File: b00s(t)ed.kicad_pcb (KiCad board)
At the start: 2 copper layers, 21 x 19 mm, 10 parts, among them Q1 IRF7739L1, Q2 2N7002W, U1 LM5050-1, U2 NSI50010YT1G

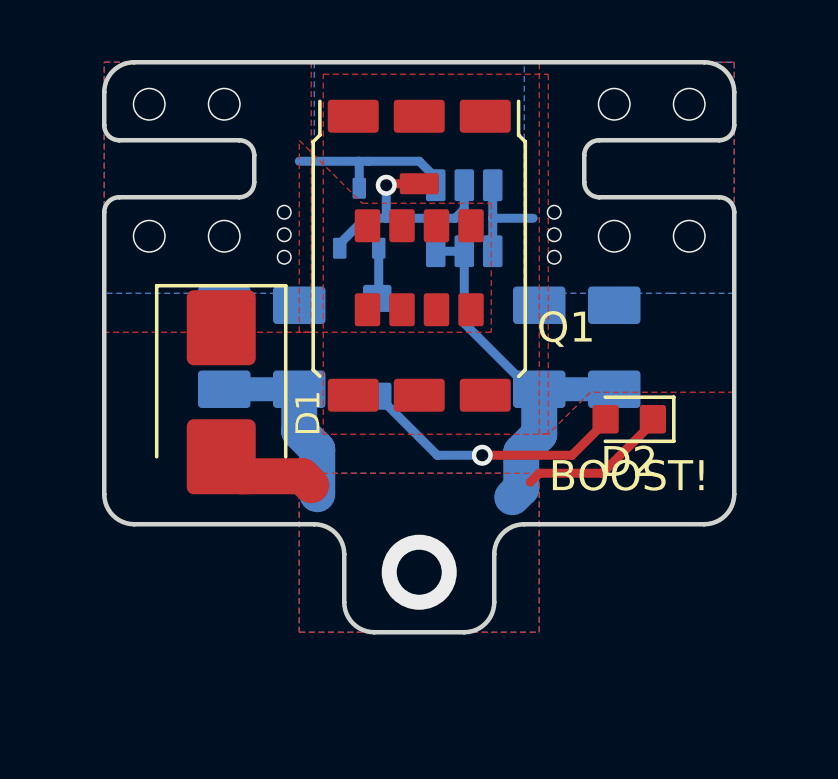
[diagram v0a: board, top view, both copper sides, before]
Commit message: Wire tabs update
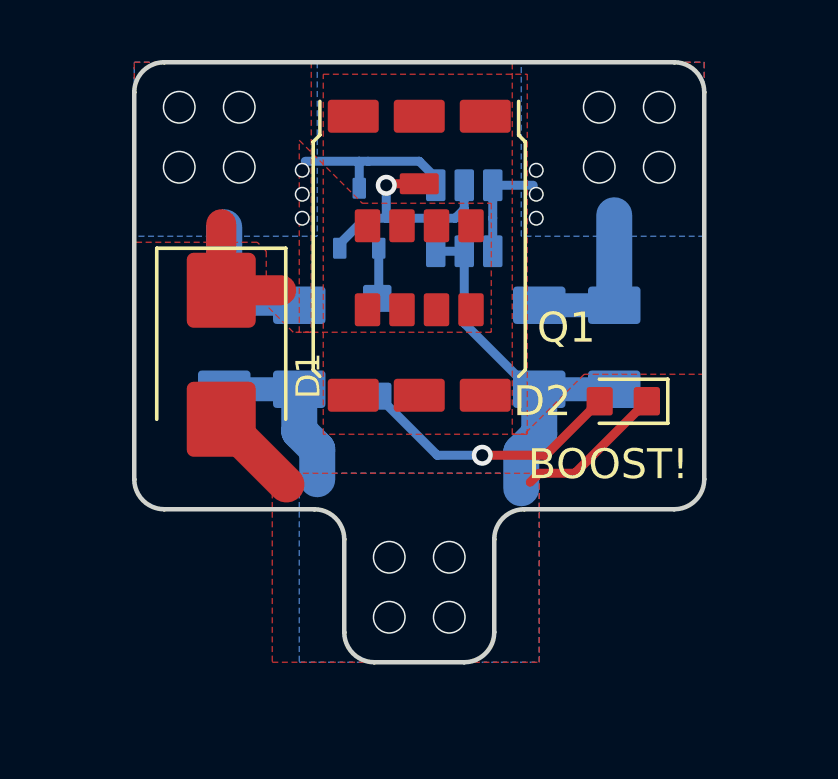
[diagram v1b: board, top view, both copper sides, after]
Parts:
- moved D1 1.25 mm to (133.4, 69.8)
- moved D2 0.63 mm to (146.8, 71.3)
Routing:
- net +BATT: track 5.93 -> 15.0 mm
- net /OUT: track 3.55 -> 9.05 mm
- net -BATT: track 27.7 -> 26.5 mm, vias 1 -> 4
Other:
- board size 21 x 19 mm -> 19 x 20 mm
- board text added: "2019-02-19"
- board text removed: "2019-02-12"

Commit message: 7x7mm pads
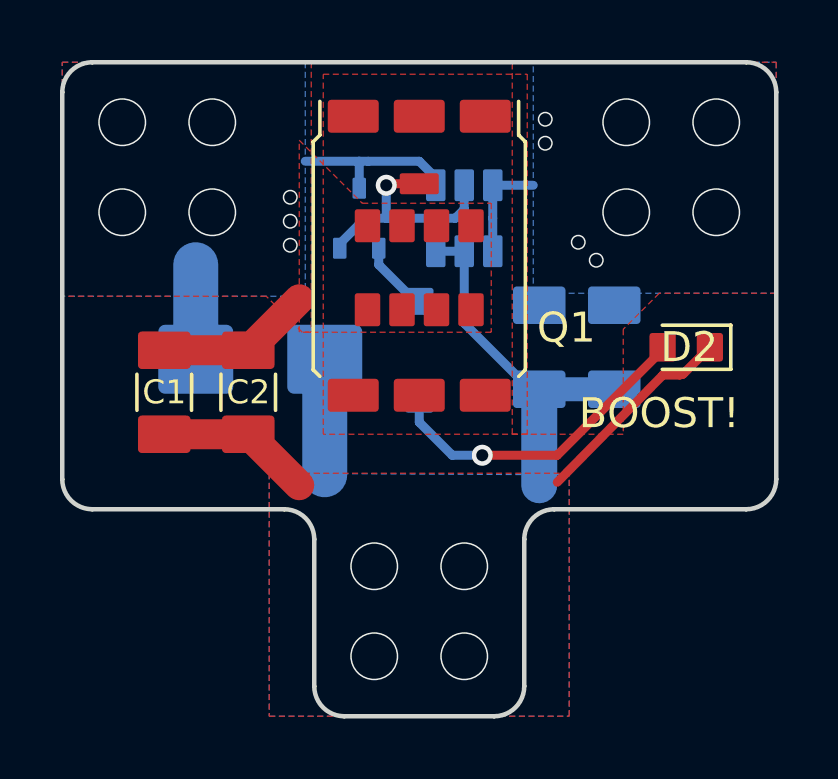
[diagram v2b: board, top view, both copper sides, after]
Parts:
- C1, C2: moved to F.Cu
- D1: moved to B.Cu
- moved D2 2.77 mm to (148.9, 69.5)
- moved C1 2.50 mm to (131.5, 71.0)
- moved C2 2.27 mm to (134.3, 71.0)
- moved U2 1.40 mm to (140.0, 69.6)
- moved D1 1.31 mm to (134.7, 69.9), turned to 0 degrees
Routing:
- net /OUT: track 9.05 -> 3.55 mm, vias 7 -> 8
- net -BATT: track 26.5 -> 28.5 mm
- net Net-(D2-Pad2): track 8.97 -> 10.9 mm
- net +BATT: track 15.0 -> 14.1 mm
- net Net-(Q2-Pad1): track 1.69 -> 2.41 mm
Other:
- board size 19 x 20 mm -> 23.8 x 21.8 mm
- board text added: "+IN 2-6s→"
- board text added: "+OUT"
- board text removed: "2-6s"

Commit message: Fucking kicad has pin mappings wrong
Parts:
- Q2: footprint Package_TO_SOT_SMD:SOT-323_SC-70 -> Package_TO_SOT_SMD:SOT-323_SC-70-FET
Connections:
- U1 pad 5: Net-(Q1-Pad2) -> Net-(Q1-PadG)
- U2 pad A: Net-(Q2-Pad1) -> Net-(Q2-PadS)
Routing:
- net Net-(Q1-Pad2): track 7.80 -> 0.00 mm, vias 1 -> 0
- net Net-(Q1-PadG): track 0.00 -> 6.85 mm, vias 0 -> 1
- net Net-(Q2-PadS): track 0.00 -> 3.71 mm
- net Net-(Q2-Pad1): track 2.41 -> 0.00 mm
- net Net-(D2-Pad2): track 10.9 -> 9.96 mm
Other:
- board text added: "+IN 2-6S→"
- board text added: "2019-03-12"
- board text removed: "+IN 2-6s→"
- board text removed: "2019-02-19"
